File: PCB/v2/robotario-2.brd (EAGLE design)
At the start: 41.7 x 49.4 mm, 27 parts, among them T1 2N3904, T2 2N3904, U1 ATTINY85-20PU

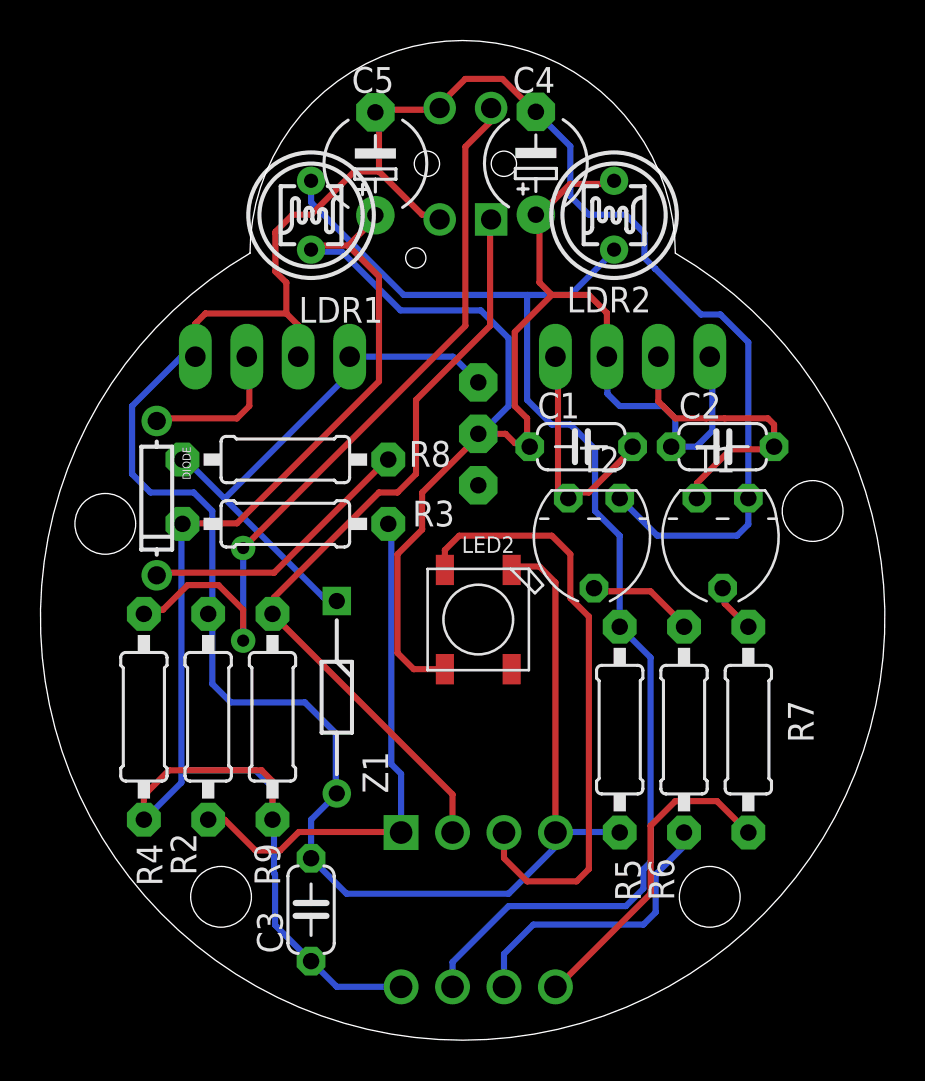
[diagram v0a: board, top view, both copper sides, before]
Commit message: added software tests
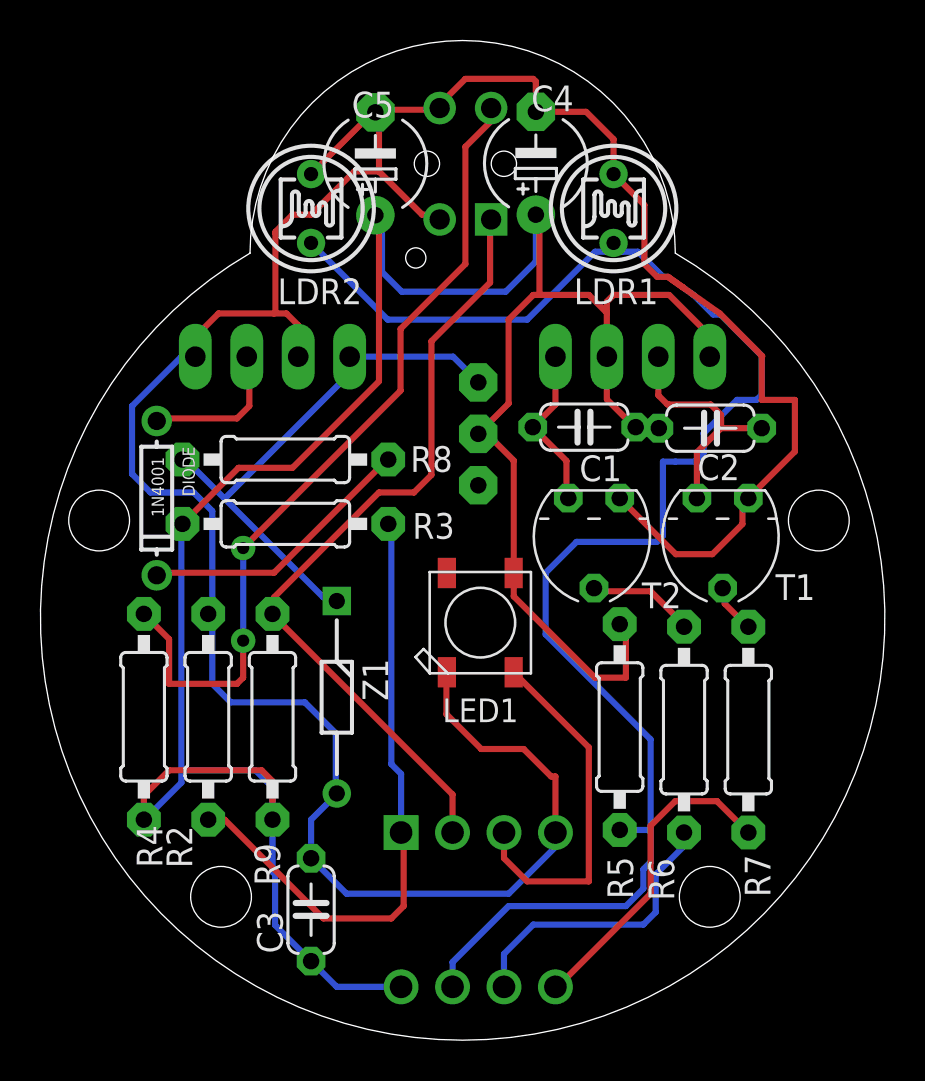
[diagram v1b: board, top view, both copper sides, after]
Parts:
- removed LED2: WS2812B5050, WS2812B:WS2812B
- added LED1: WS2812B5050, WS2812B:WS2812B
- DIODE: value (none) -> 1N4001
- R4: value 100 -> 1k
- moved LDR2 15.0 mm to (12.5, 40.2), turned to 90 degrees
- moved LDR1 14.9 mm to (27.4, 40.2)
- moved C2 1.10 mm to (32.2, 29.4)
- moved C1 0.98 mm to (26.0, 29.4), turned to 180 degrees
- moved R5 0.13 mm to (27.7, 14.6)
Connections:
- net GND: now also LDR1.2, LDR2.2, LED1.3-GND; no longer LED2.3-GND, R5.2
- net N$6: now also LDR1.1, LDR2.1, R5.2; no longer LDR1.2, LDR2.2, R5.1
- net N$9: now also LED1.4-DIN; no longer LED2.4-DIN
- net VCC: now also LED1.1-VDD, R5.1; no longer LDR1.1, LDR2.1, LED2.1-VDD
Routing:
- net N$6: track 63.6 -> 78.4 mm
- net N$9: track 30.0 -> 17.8 mm
- net VCC: track 139.8 -> 129.8 mm
- net N$4: track 26.0 -> 31.1 mm
- net N$10: track 12.5 -> 8.17 mm
- net N$7: track 15.1 -> 12.0 mm
- net GND: track 137.2 -> 139.7 mm
- net N$15: track 39.0 -> 40.9 mm
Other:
- board text added: "Design by Y.G. & R.C."
- board text removed: "Design by Y.G."

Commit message: changed resistor
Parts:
- R9: value 5k -> 10k
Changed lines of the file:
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@@
 <attribute name="NAME" x="5.1562" y="7.6962" size="1.27" layer="25" ratio="12" rot="R90"/>
 </element>
-<element name="R9" library="adafruit" library_urn="urn:adsk.eagle:library:420" package="0207/10" package3d_urn="urn:adsk.eagle:package:6240597/1" value="5k" x="10.5918" y="15.1384" smashed="yes" rot="R90">
+<element name="R9" library="adafruit" library_urn="urn:adsk.eagle:library:420" package="0207/10" package3d_urn="urn:adsk.eagle:package:6240597/1" value="10k" x="10.5918" y="15.1384" smashed="yes" rot="R90">
 <attribute name="NAME" x="10.9728" y="6.8072" size="1.27" layer="25" ratio="12" rot="R90"/>
 </element>
